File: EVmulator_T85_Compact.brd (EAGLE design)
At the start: 23 x 13 mm, 24 parts, among them Q2 DMN3404L-7, U1 ATTINY85V

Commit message: Finished compact version
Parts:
- moved C1 8.56 mm to (12.0, 10.0)
- moved C2 8.56 mm to (12.0, 8.00)
- moved C3 8.56 mm to (6.50, 3.50)
- moved D1 8.56 mm to (21.0, 10.0)
- moved D2 8.56 mm to (6.00, 1.50)
- moved D3 8.56 mm to (13.0, 2.50)
- moved D4 8.56 mm to (11.5, 12.0)
- moved J1 8.56 mm to (9.50, 9.50)
- moved Q2 8.56 mm to (8.00, 11.0)
- moved R1 8.56 mm to (7.00, 8.00)
- moved R10 8.56 mm to (5.00, 11.0)
- moved R2 8.56 mm to (7.00, 6.00)
- moved R3 8.56 mm to (21.0, 6.00)
- moved R4 8.56 mm to (21.0, 4.00)
- moved R5 8.56 mm to (10.5, 1.50)
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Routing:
- net CON_CP: track 5.97 -> 37.4 mm, vias 0 -> 3
- net LED_GN: track 0.00 -> 18.9 mm, vias 0 -> 1
- net N$10: track 0.00 -> 15.9 mm, vias 0 -> 2
- net LED_RD: track 0.00 -> 15.1 mm, vias 0 -> 1
- net N$5: track 3.81 -> 15.9 mm, vias 0 -> 2
- net PWM_DET: track 8.92 -> 17.8 mm
- net N$3: track 0.00 -> 6.55 mm, vias 0 -> 1
- net N$4: track 0.00 -> 6.37 mm, vias 0 -> 1
- net 4V7: track 11.5 -> 16.0 mm, vias 0 -> 1
- net N$1: track 0.00 -> 3.52 mm, vias 0 -> 1
- net N$2: track 0.00 -> 3.27 mm, vias 0 -> 1
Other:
- board text added: "25A"
- board text added: "GND"
- board text removed: "32A"
- board text removed: "GN"

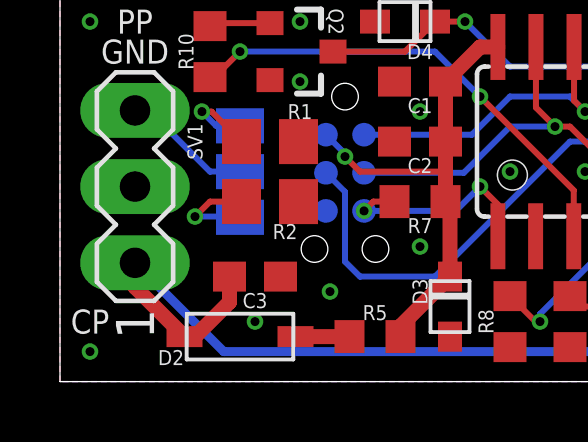
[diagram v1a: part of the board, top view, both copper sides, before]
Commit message: changed silkscreen for the 3pin header on both boards. Updated gerbers.
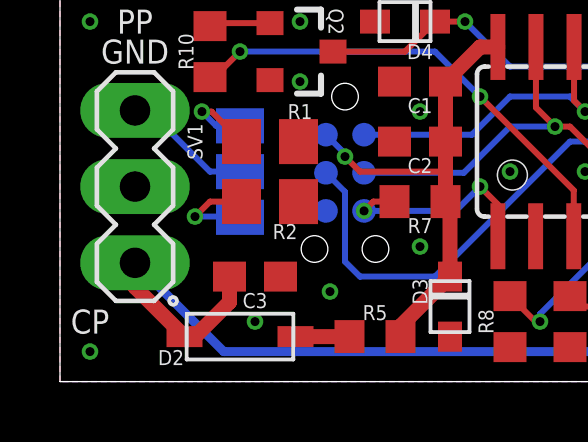
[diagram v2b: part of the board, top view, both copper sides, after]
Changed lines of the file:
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@@
 <drawing>
 <settings>
-<setting alwaysvectorfont="yes"/>
+<setting alwaysvectorfont="no"/>
 <setting verticaltext="up"/>
 </settings>
@@
 <attribute name="VALUE" x="19.5" y="19" size="1.27" layer="27" ratio="10" rot="R90"/>
 </element>
-<element name="SV1" library="con-lstb" library_urn="urn:adsk.eagle:library:162" package="MA03-1" package3d_urn="urn:adsk.eagle:package:8339/1" value="" x="2.5" y="6.5" smashed="yes" rot="R90">
+<element name="SV1" library="con-lstb" library_urn="urn:adsk.eagle:library:41989194" package="MA03-1" package3d_urn="urn:adsk.eagle:package:43315831/1" value="" x="2.5" y="6.5" smashed="yes" rot="R90">
 <attribute name="MF" value="" x="2.5" y="6.5" size="1.27" layer="27" rot="R90" display="off"/>
 <attribute name="MPN" value="" x="2.5" y="6.5" size="1.27" layer="27" rot="R90" display="off"/>
